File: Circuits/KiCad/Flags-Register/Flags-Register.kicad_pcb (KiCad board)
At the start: 2 copper layers, 77.5 x 55.9 mm, 16 parts, among them J1 Conn_01x18_Male, J2 Conn_01x02_Male, J3 Conn_01x02_Male, U1 74x08, U2 74x08, U3 74x32, U4 74x32, U5 74x04, U6 74x74, U7 74x74

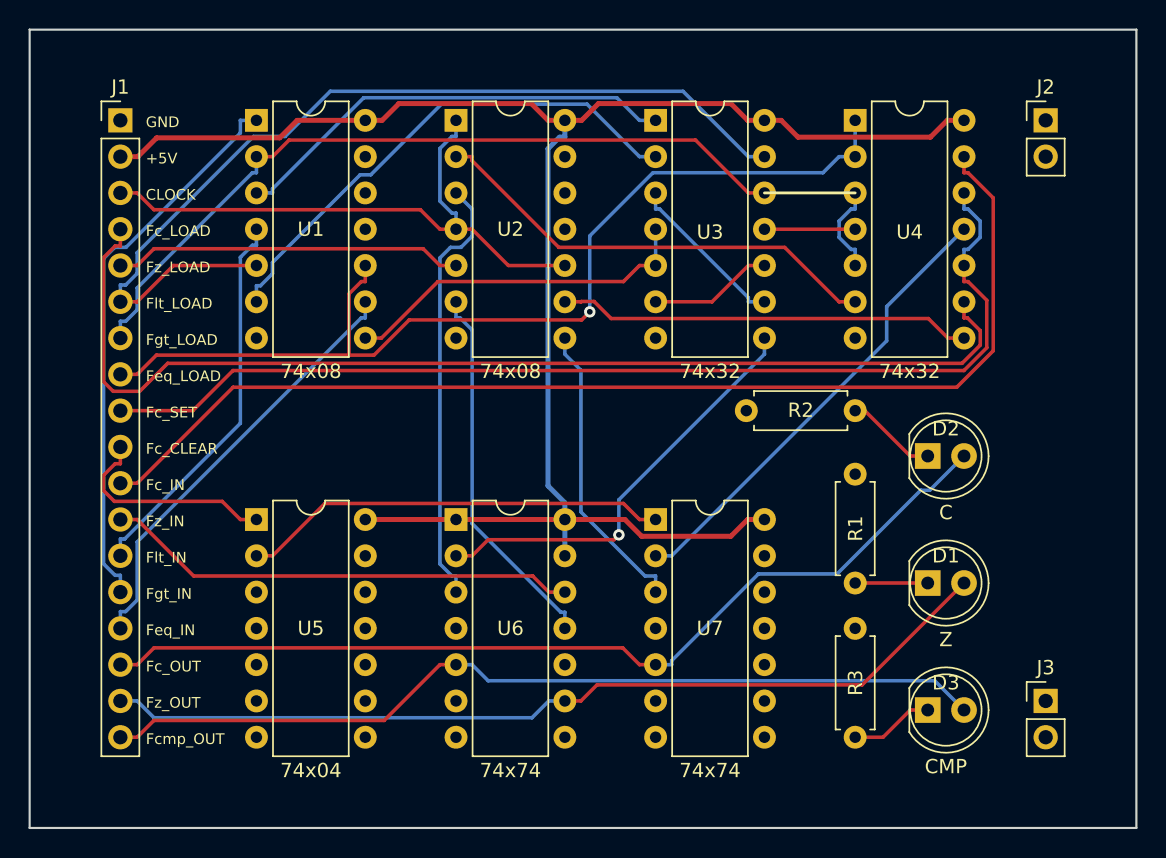
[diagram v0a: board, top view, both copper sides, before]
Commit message: Finished Flag Register schematic & PCB
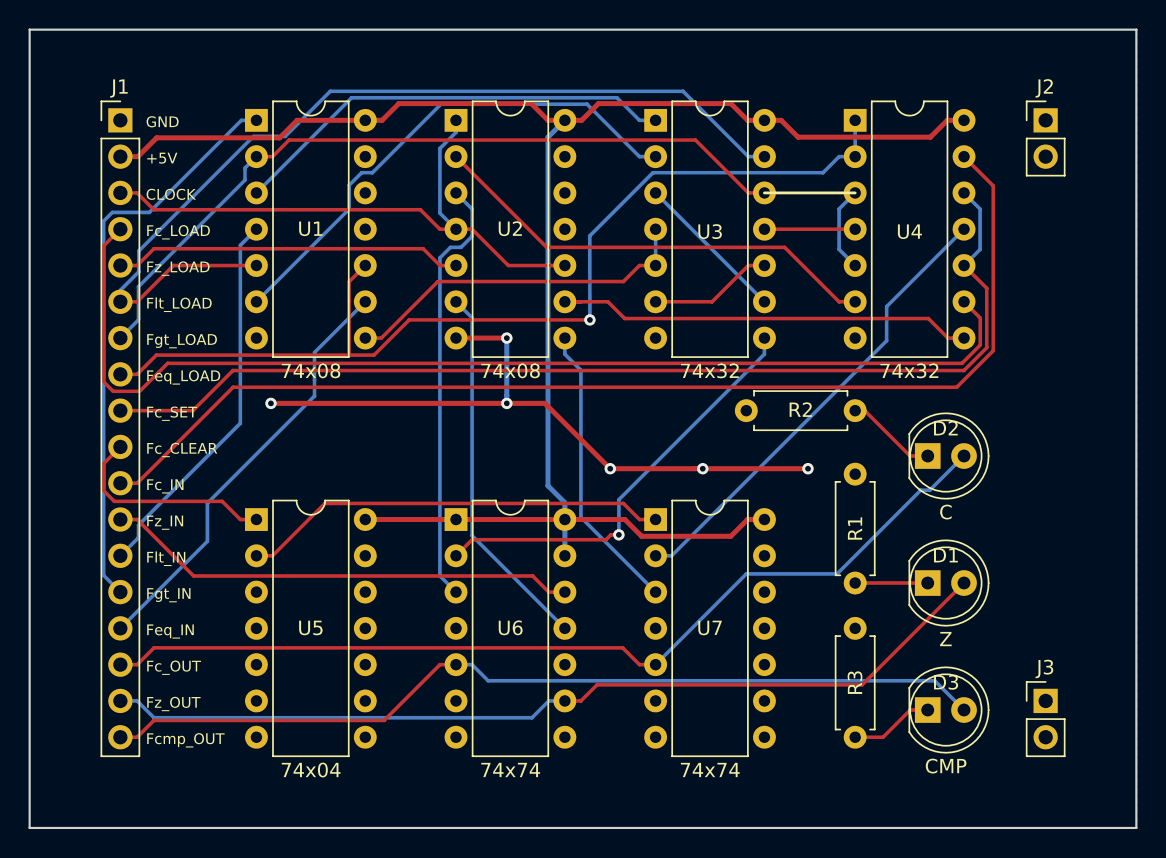
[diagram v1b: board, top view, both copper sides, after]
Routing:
- net GND: track 0.00 -> 47.6 mm, vias 0 -> 6
- net Net-(U2-Pad9): track 29.0 -> 30.1 mm
- net Net-(U3-Pad3): track 11.6 -> 10.8 mm
- net Fgt_IN: track 39.3 -> 40.1 mm

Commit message: Made sure spacing between headers is always 2.54mm pitch
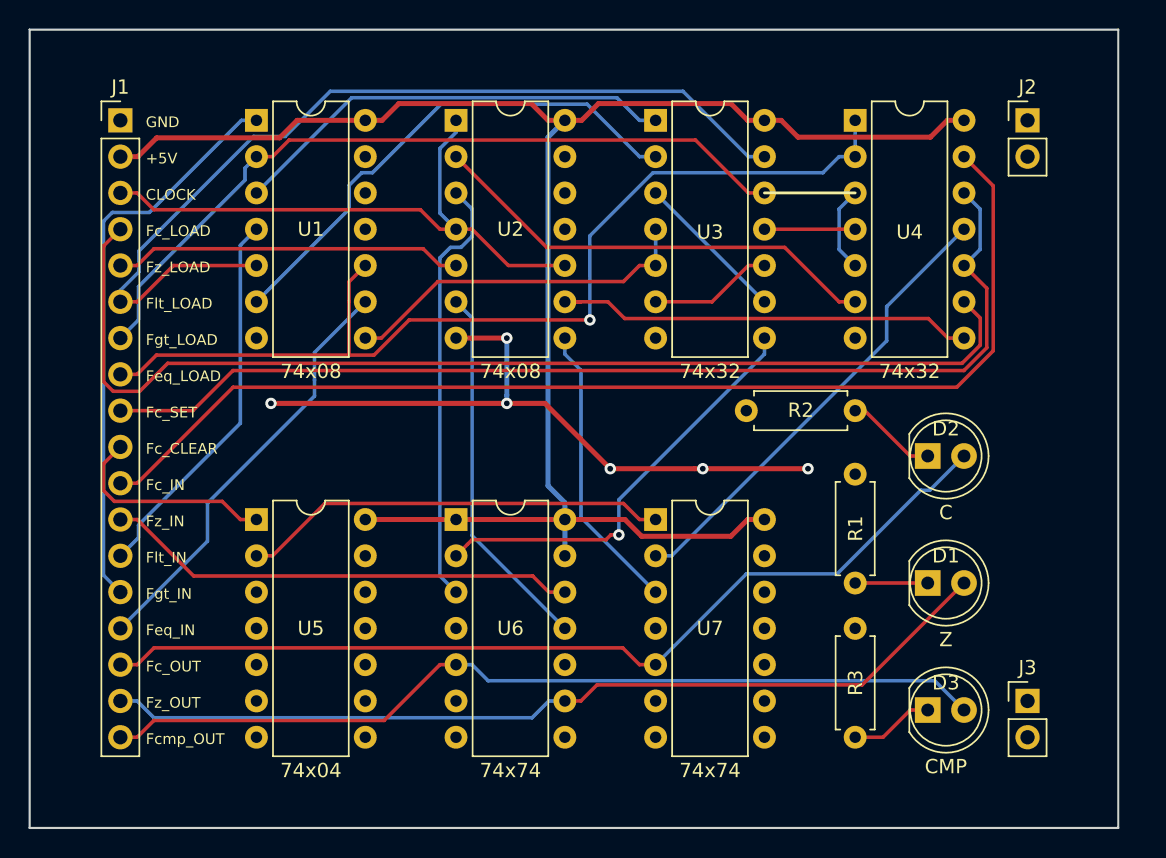
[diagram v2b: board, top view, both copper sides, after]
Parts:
- moved J2 1.27 mm to (109.2, 45.7)
- moved J3 1.27 mm to (109.2, 86.4)
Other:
- board size 77.5 x 55.9 mm -> 76.2 x 55.9 mm
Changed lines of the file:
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@@
   )
   (module Connector_PinHeader_2.54mm:PinHeader_1x02_P2.54mm_Vertical (layer F.Cu)
-    (at 110.49 45.72)
+    (at 109.22 45.72)
     (descr "Through hole straight pin header, 1x02, 2.54mm pitch, single row")
     (tags "Through hole pin header THT 1x02 2.54mm single row")
@@
   )
   (module Connector_PinHeader_2.54mm:PinHeader_1x02_P2.54mm_Vertical (layer F.Cu)
-    (at 110.49 86.36)
+    (at 109.22 86.36)
     (descr "Through hole straight pin header, 1x02, 2.54mm pitch, single row")
     (tags "Through hole pin header THT 1x02 2.54mm single row")
@@
   )
   (gr_line (start 39.37 95.25) (end 39.37 39.37) (layer Edge.Cuts) (width 0.15))
-  (gr_line (start 116.84 95.25) (end 39.37 95.25) (layer Edge.Cuts) (width 0.15))
-  (gr_line (start 116.84 39.37) (end 116.84 95.25) (layer Edge.Cuts) (width 0.15))
-  (gr_line (start 39.37 39.37) (end 116.84 39.37) (layer Edge.Cuts) (width 0.15))
+  (gr_line (start 115.57 95.25) (end 39.37 95.25) (layer Edge.Cuts) (width 0.15))
+  (gr_line (start 115.57 39.37) (end 115.57 95.25) (layer Edge.Cuts) (width 0.15))
+  (gr_line (start 39.37 39.37) (end 115.57 39.37) (layer Edge.Cuts) (width 0.15))
   (gr_poly (pts (xy 39.45 39.45) (xy 44.45 39.45) (xy 44.45 44.45) (xy 39.45 44.45)) (layer Margin) (width 0.15))
   (gr_poly (pts (xy 39.45 90.17) (xy 44.45 90.17) (xy 44.45 95.17) (xy 39.45 95.17)) (layer Margin) (width 0.15))
-  (gr_poly (pts (xy 111.76 90.25) (xy 116.76 90.25) (xy 116.76 95.25) (xy 111.76 95.25)) (layer Margin) (width 0.15))
-  (gr_poly (pts (xy 111.76 39.45) (xy 116.76 39.45) (xy 116.76 44.45) (xy 111.76 44.45)) (layer Margin) (width 0.15))
+  (gr_poly (pts (xy 110.49 90.17) (xy 115.49 90.17) (xy 115.49 95.17) (xy 110.49 95.17)) (layer Margin) (width 0.15))
+  (gr_poly (pts (xy 110.49 39.45) (xy 115.49 39.45) (xy 115.49 44.45) (xy 110.49 44.45)) (layer Margin) (width 0.15))
   (gr_line (start 90.805 50.8) (end 97.155 50.8) (layer F.SilkS) (width 0.2))
   (gr_text Fcmp_OUT (at 47.498 89.027) (layer F.SilkS)
@@
     (polygon
       (pts
-        (xy 39.37 39.37) (xy 116.84 39.37) (xy 116.84 95.25) (xy 39.37 95.25)
+        (xy 39.37 39.37) (xy 115.57 39.37) (xy 115.57 95.25) (xy 39.37 95.25)
       )
     )

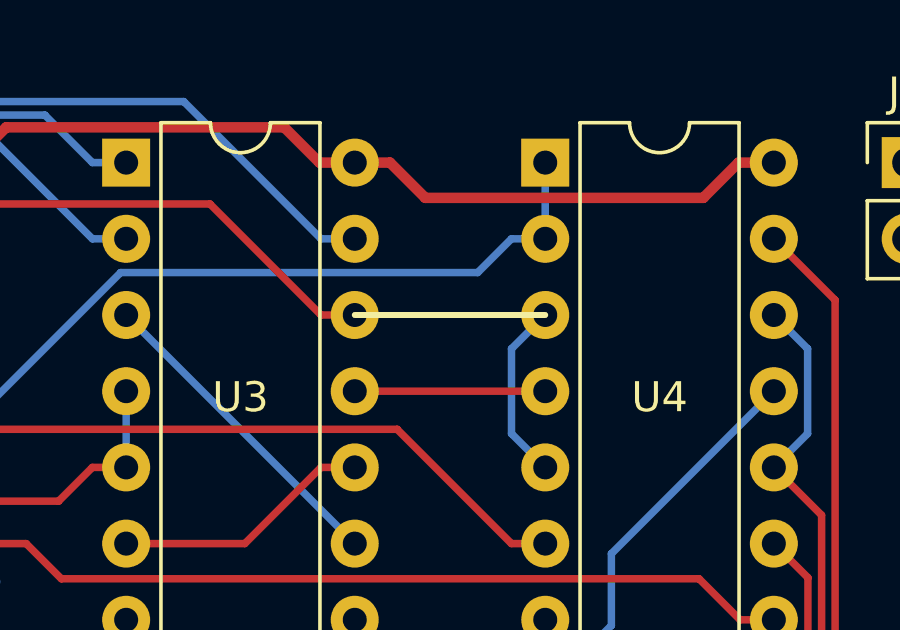
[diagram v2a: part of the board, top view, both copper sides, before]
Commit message: Rerouted Controller and Main board (needs work)
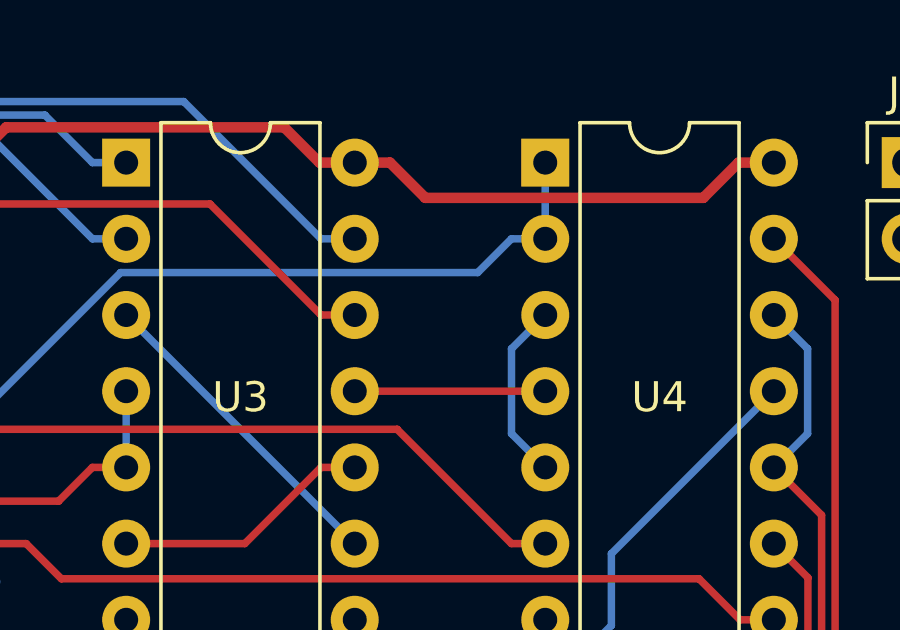
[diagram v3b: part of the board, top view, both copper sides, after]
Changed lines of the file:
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@@
-(kicad_pcb (version 20171130) (host pcbnew 5.0.2+dfsg1-1)
+(kicad_pcb (version 20171130) (host pcbnew "(5.1.2)-2")
   (general
     (thickness 1.6)
-    (drawings 27)
+    (drawings 26)
     (tracks 264)
     (zones 0)
@@
     (zone_45_only no)
     (trace_min 0.2)
-    (segment_width 0.2)
-    (edge_width 0.15)
     (via_size 0.8)
     (via_drill 0.4)
@@
     (uvia_min_size 0.2)
     (uvia_min_drill 0.1)
+    (edge_width 0.15)
+    (segment_width 0.2)
     (pcb_text_width 0.3)
     (pcb_text_size 1.5 1.5)
@@
     (solder_mask_min_width 0.25)
     (aux_axis_origin 0 0)
-    (visible_elements FFFFFF7F)
+    (visible_elements 7FFFFFFF)
     (pcbplotparams
       (layerselection 0x010fc_ffffffff)
@@
   (gr_poly (pts (xy 110.49 90.17) (xy 115.49 90.17) (xy 115.49 95.17) (xy 110.49 95.17)) (layer Margin) (width 0.15))
   (gr_poly (pts (xy 110.49 39.45) (xy 115.49 39.45) (xy 115.49 44.45) (xy 110.49 44.45)) (layer Margin) (width 0.15))
-  (gr_line (start 90.805 50.8) (end 97.155 50.8) (layer F.SilkS) (width 0.2))
   (gr_text Fcmp_OUT (at 47.498 89.027) (layer F.SilkS)
     (effects (font (size 0.75 0.75) (thickness 0.15)) (justify left))
